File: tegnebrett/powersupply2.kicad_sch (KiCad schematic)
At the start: 41 parts, among them J7 PJ-002A, U3 TPS54294PWP1, U4 TPS54294PWP2

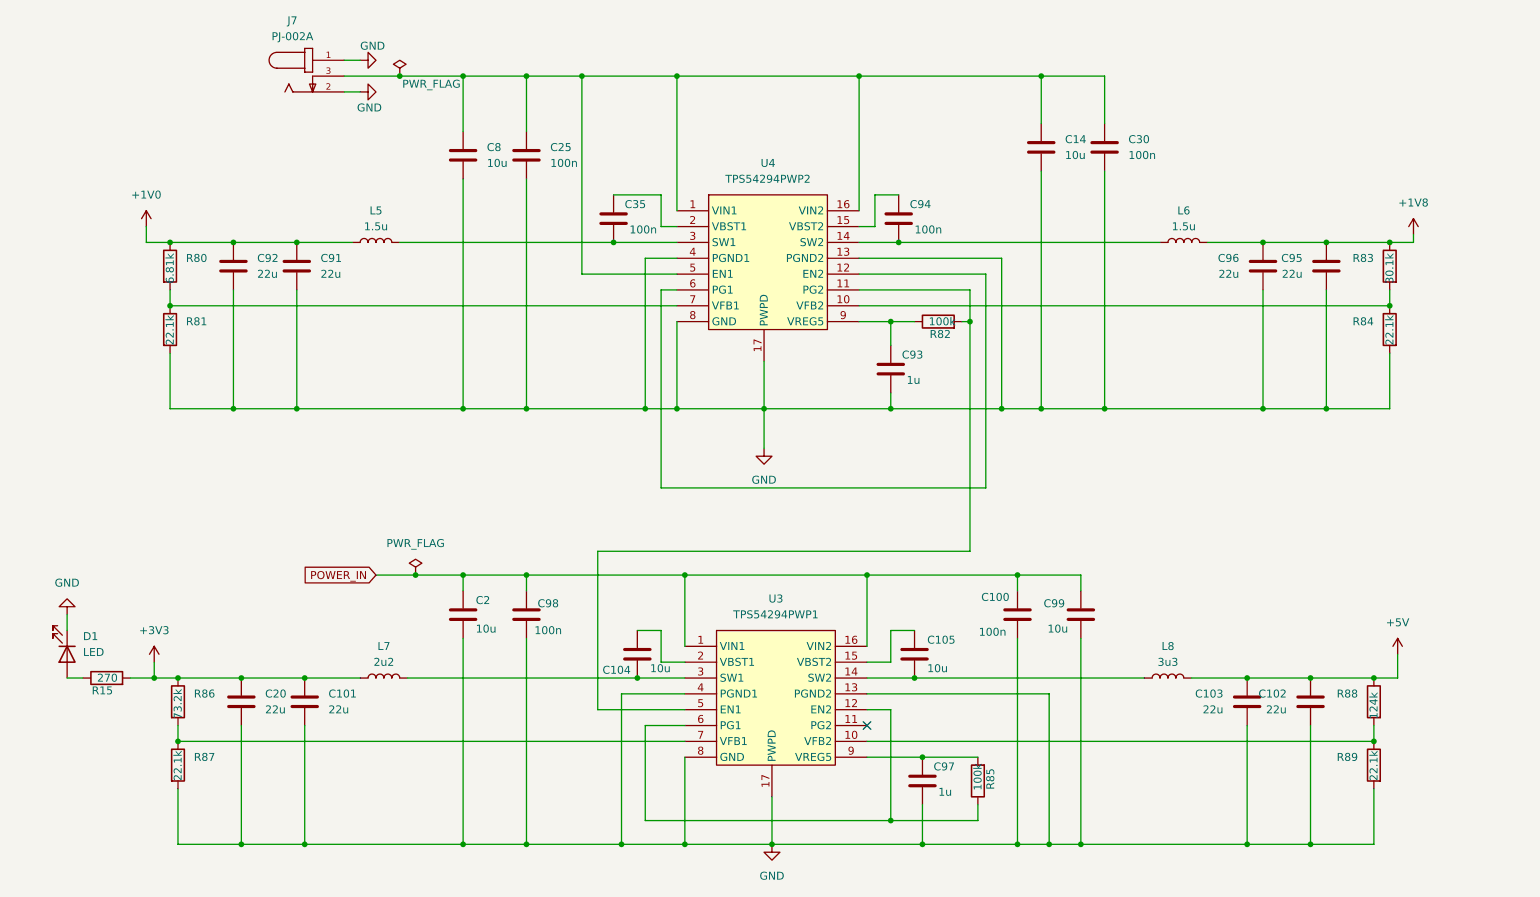
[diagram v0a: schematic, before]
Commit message: feat: add jumpers to PowerSupply schematic
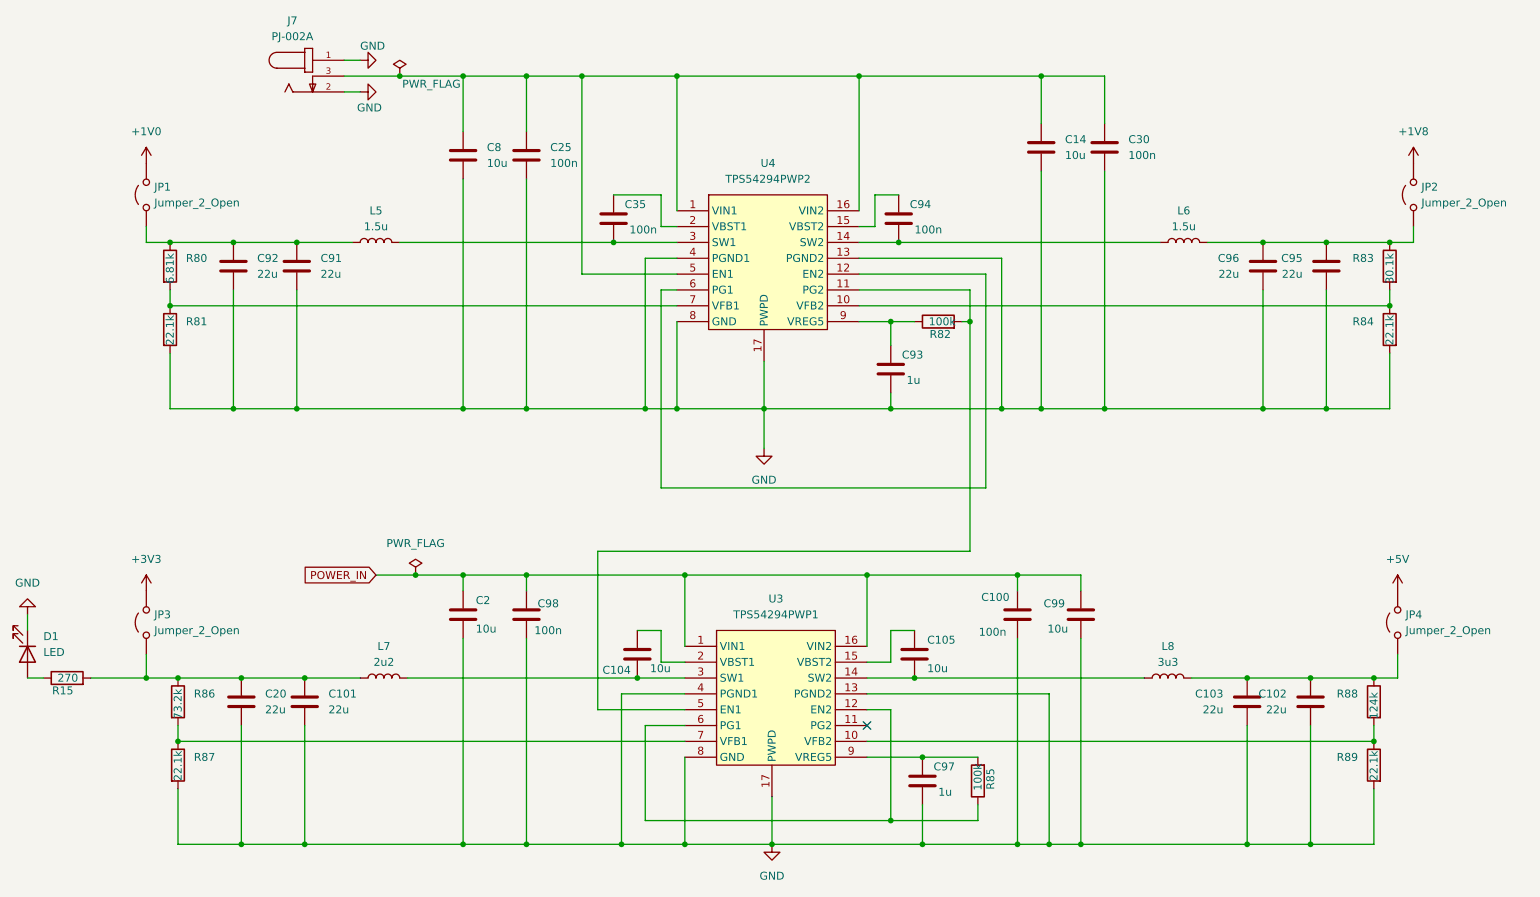
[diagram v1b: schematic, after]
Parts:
- added JP1, JP2, JP3, JP4: Jumper_2_Open, symbol Jumper:Jumper_2_Open
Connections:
- net +1V0: now also JP1.2 (B); no longer C91.1, C92.1, L5.1, R80.1
- net +1V8: now also JP2.2 (B); no longer C95.1, C96.1, L6.1, R83.1
- net +3V3: now also JP3.2 (B); no longer C101.1, C20.1, L7.1, R15.2, R86.1
- net +5V: now also JP4.2 (B); no longer C102.1, C103.1, L8.1, R88.1
- new net: C95.1, C96.1, JP2.1 (A), L6.1, R83.1
- new net: C101.1, C20.1, JP3.1 (A), L7.1, R15.2, R86.1
- new net: C91.1, C92.1, JP1.1 (A), L5.1, R80.1
- new net: C102.1, C103.1, JP4.1 (A), L8.1, R88.1
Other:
- moved on the sheet: D1, R15

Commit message: feat: add footprint to jumper and import to PCB
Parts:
- JP1, JP2, JP3, JP4: footprint (none) -> Connector_PinHeader_2.54mm:PinHeader_1x02_P2.54mm_Vertical
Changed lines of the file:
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@@
 			)
 		)
-		(property "Footprint" ""
+		(property "Footprint" "Connector_PinHeader_2.54mm:PinHeader_1x02_P2.54mm_Vertical"
 			(at 52.07 115.57 0)
 			(effects
@@
 			)
 		)
-		(property "Footprint" ""
+		(property "Footprint" "Connector_PinHeader_2.54mm:PinHeader_1x02_P2.54mm_Vertical"
 			(at 255.27 46.99 0)
 			(effects
@@
 			)
 		)
-		(property "Footprint" ""
+		(property "Footprint" "Connector_PinHeader_2.54mm:PinHeader_1x02_P2.54mm_Vertical"
 			(at 52.07 46.99 0)
 			(effects
@@
 			)
 		)
-		(property "Footprint" ""
+		(property "Footprint" "Connector_PinHeader_2.54mm:PinHeader_1x02_P2.54mm_Vertical"
 			(at 252.73 115.57 0)
 			(effects

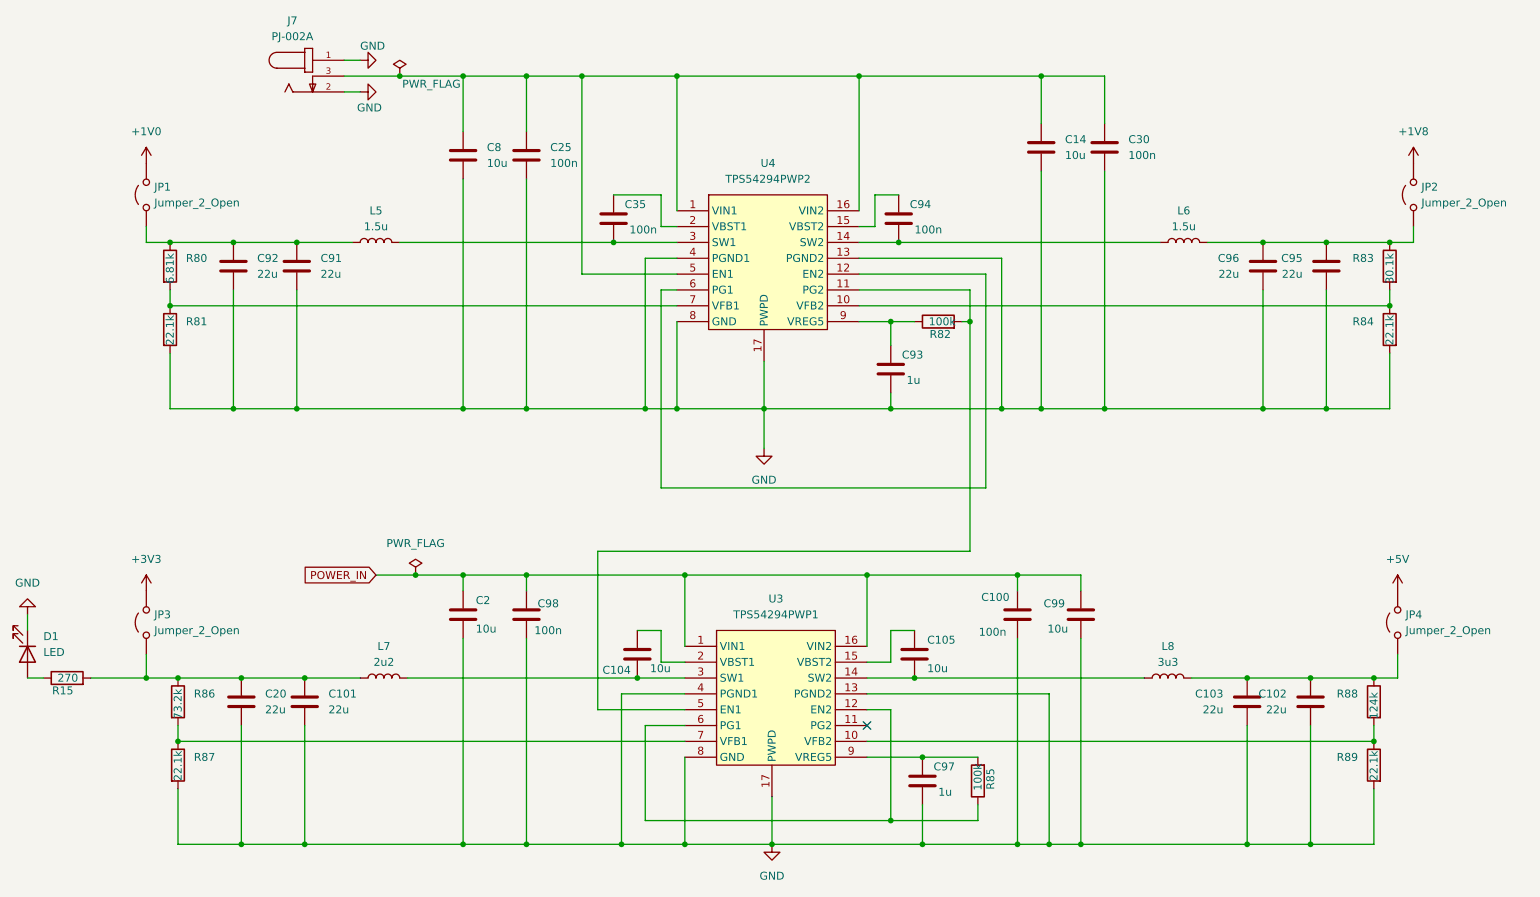
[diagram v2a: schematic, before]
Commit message: refactor: re-annotate schematic labels
References for schematic capacitors (for example C74 -> C2), etc.
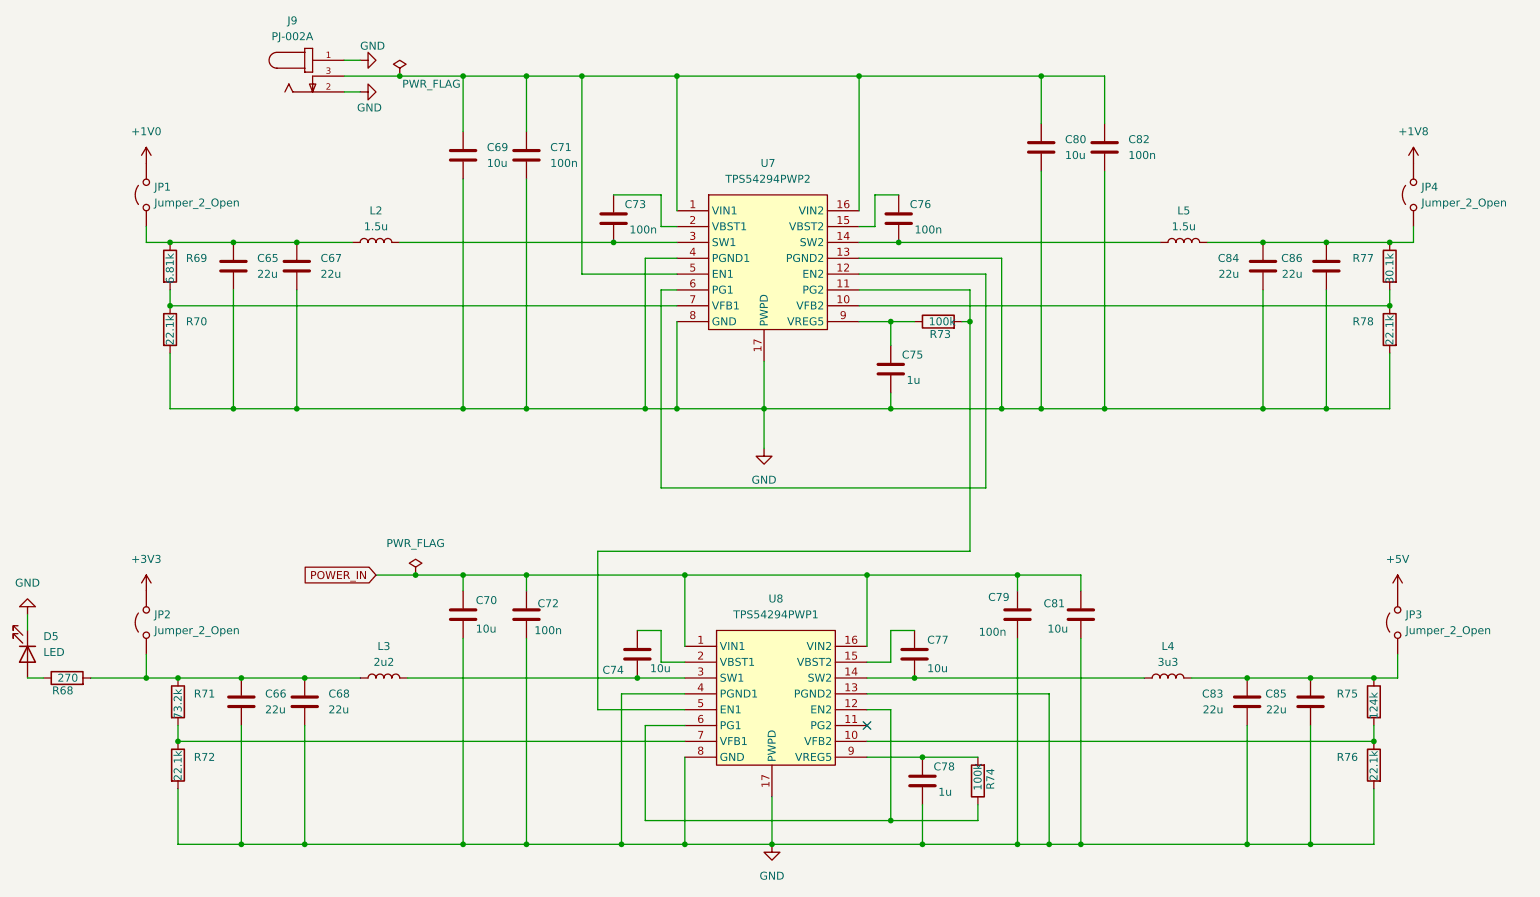
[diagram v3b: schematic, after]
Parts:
- renumbered C92 to C65, C20 to C66, C91 to C67, C101 to C68, C8 to C69, C2 to C70, C25 to C71, C98 to C72, C35 to C73, C104 to C74, C93 to C75, C94 to C76, C105 to C77, C97 to C78, C100 to C79, C14 to C80, C99 to C81, C30 to C82, C103 to C83, C96 to C84, C102 to C85, C95 to C86, D1 to D5, J7 to J9, JP3 to JP2, JP4 to JP3, JP2 to JP4, L5 to L2, L7 to L3, L8 to L4, L6 to L5, R15 to R68, R80 to R69, R81 to R70, R86 to R71, R87 to R72, R82 to R73, R85 to R74, R88 to R75, R89 to R76, R83 to R77, R84 to R78, U4 to U7, U3 to U8

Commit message: schematic: some smaller updates
I am not entirely sure what was updated, but surely not antyhing huge.
From the diff we can read that it's perhaps the symbols which got an
update.
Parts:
- J9: footprint tegnebrett_modules:CUI_PJ-002A -> CUI_PJ-002A; symbol power_jack:PJ-002A -> tegnebrett_symbols:PJ-002A
- U7, U8: symbol Tegnebrettsymbol:TPS54294PWP -> tegnebrett_symbols:TPS54294PWP
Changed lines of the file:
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@@
 	)
 	(symbol
-		(lib_id "power_jack:PJ-002A")
+		(lib_id "tegnebrett_symbols:PJ-002A")
 		(at 78.74 27.94 0)
 		(unit 1)
@@
 			)
 		)
-		(property "Footprint" "tegnebrett_modules:CUI_PJ-002A"
+		(property "Footprint" "CUI_PJ-002A"
 			(at 78.74 27.94 0)
 			(effects
@@
 	)
 	(symbol
-		(lib_id "Tegnebrettsymbol:TPS54294PWP")
+		(lib_id "tegnebrett_symbols:TPS54294PWP")
 		(at 142.24 46.99 0)
 		(unit 1)
@@
 	)
 	(symbol
-		(lib_id "Tegnebrettsymbol:TPS54294PWP")
+		(lib_id "tegnebrett_symbols:TPS54294PWP")
 		(at 143.51 116.84 0)
 		(unit 1)
